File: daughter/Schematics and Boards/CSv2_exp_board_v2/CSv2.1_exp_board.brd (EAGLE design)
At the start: 38.1 x 47 mm, 103 parts, among them J1 HIROSE-DF40_50-PIN_CONNECTORS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, J3 CORTEX_DEBUG_SMD, J4 SJ-43514-SMTC, J6 ATTINY_AVR_DEBUG, J7 J-USB-HIROSE-MICRO-USB, SW1 SPST_TACT-KMR2, SW2 SPST_TACT-KMR2, U1 LOADSWITCH-MIC94164, U10 LOADSWITCH-MIC94164, U11 BMI160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

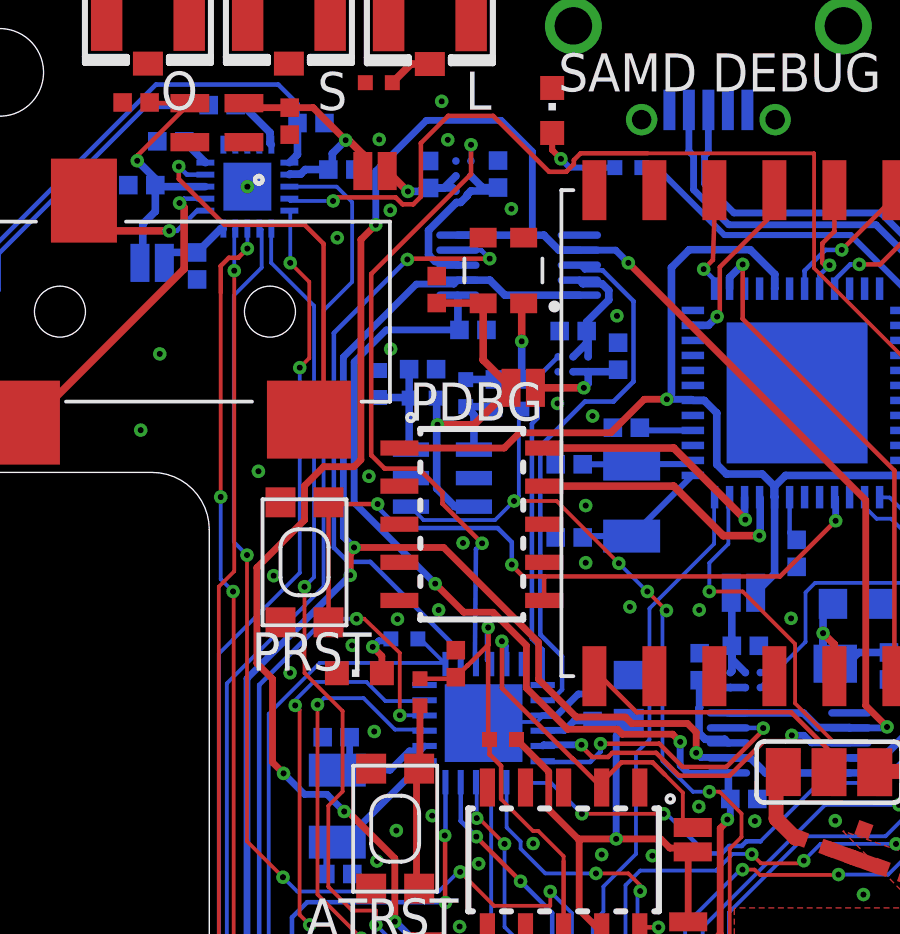
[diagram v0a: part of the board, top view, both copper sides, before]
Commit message: DTR: update SGTL5000 library part according to the SDFM
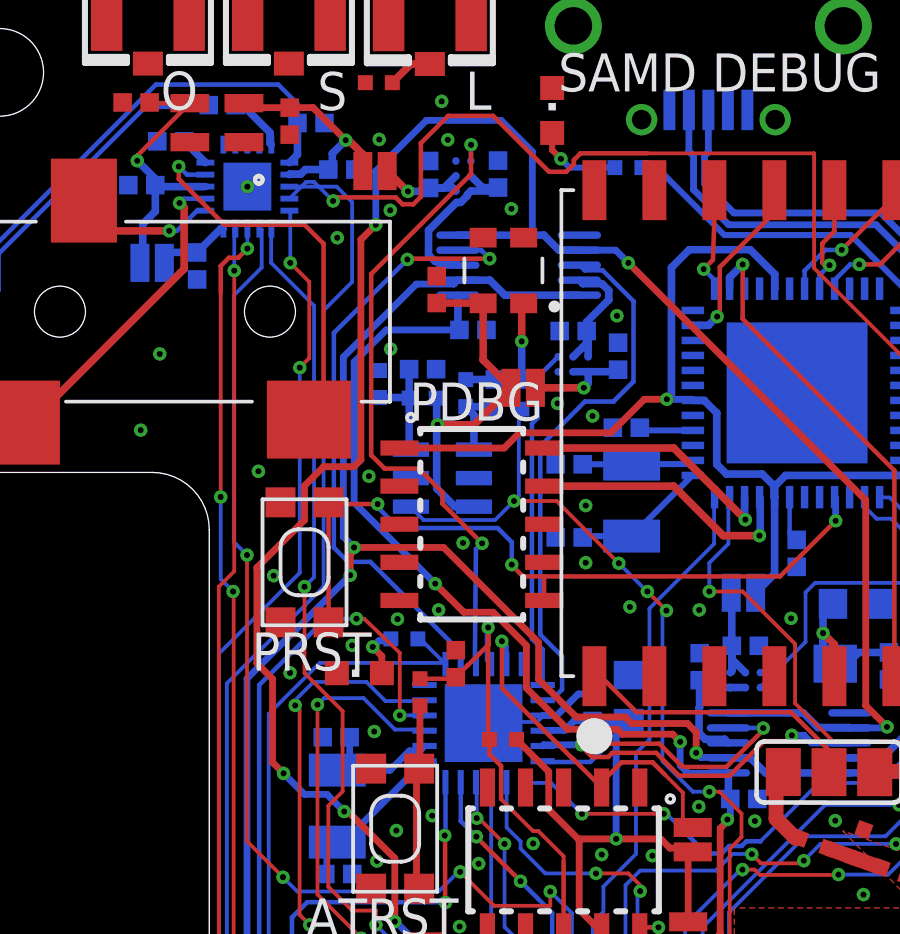
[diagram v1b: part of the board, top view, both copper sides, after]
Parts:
- U4: device CommonSense-DTR-v1:RFM-MOD -> Radios:RFM-MOD

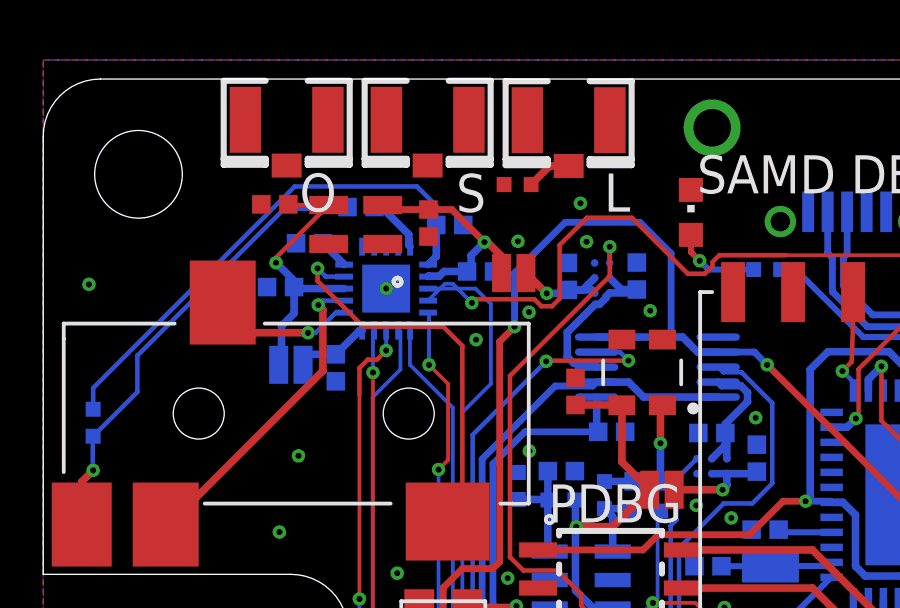
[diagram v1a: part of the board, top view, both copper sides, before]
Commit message: DTR: Regen gerbers for final design fixes in rev2.1
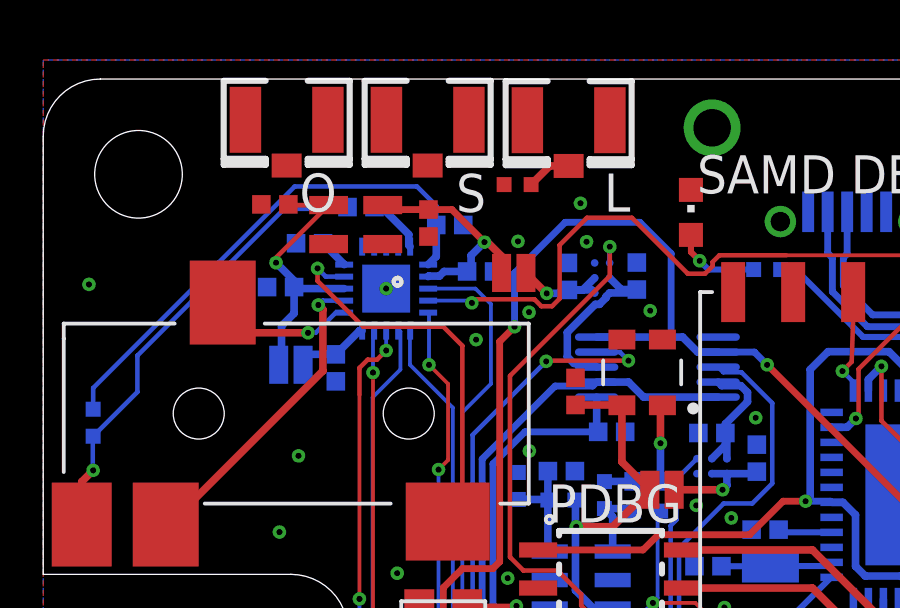
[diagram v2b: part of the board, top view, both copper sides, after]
